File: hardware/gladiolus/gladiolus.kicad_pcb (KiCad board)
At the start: 4 copper layers, 70.7 x 53.3 mm, 133 parts, among them J1 NEIGHBOR1, J2 NEIGHBOR2, J7 BONUS_ROW, P1 CONN_01X05, Q1 Q_NPN_BEC, U1 THS4520RGT, U2 AD8330ARQZ, U3 AD9283, U4 AD9704, U5 LMH6643

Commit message: Gladiolus: updated series resistor values to match those used at ShmooCon 2017
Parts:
- R38, R39, R40, R41, R42, R43, R44, R45: value 39 -> 0
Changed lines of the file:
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@@
   )
   (setup
-    (last_trace_width 1.27)
+    (last_trace_width 0.3048)
     (user_trace_width 0.3048)
     (user_trace_width 0.508)
@@
       (effects (font (size 0.6096 0.6096) (thickness 0.1524)))
     )
-    (fp_text value 39 (at 0 0) (layer F.SilkS) hide
+    (fp_text value 0 (at 0 0) (layer F.SilkS) hide
       (effects (font (size 0.6096 0.6096) (thickness 0.1524)))
     )
@@
       (effects (font (size 0.6096 0.6096) (thickness 0.1524)))
     )
-    (fp_text value 39 (at 0 0) (layer F.SilkS) hide
+    (fp_text value 0 (at 0 0) (layer F.SilkS) hide
       (effects (font (size 0.6096 0.6096) (thickness 0.1524)))
     )
@@
       (effects (font (size 0.6096 0.6096) (thickness 0.1524)))
     )
-    (fp_text value 39 (at 0 0) (layer F.SilkS) hide
+    (fp_text value 0 (at 0 0) (layer F.SilkS) hide
       (effects (font (size 0.6096 0.6096) (thickness 0.1524)))
     )
@@
       (effects (font (size 0.6096 0.6096) (thickness 0.1524)))
     )
-    (fp_text value 39 (at 0 0) (layer F.SilkS) hide
+    (fp_text value 0 (at 0 0) (layer F.SilkS) hide
       (effects (font (size 0.6096 0.6096) (thickness 0.1524)))
     )
@@
       (effects (font (size 0.6096 0.6096) (thickness 0.1524)))
     )
-    (fp_text value 39 (at 0 0) (layer F.SilkS) hide
+    (fp_text value 0 (at 0 0) (layer F.SilkS) hide
       (effects (font (size 0.6096 0.6096) (thickness 0.1524)))
     )
@@
       (effects (font (size 0.6096 0.6096) (thickness 0.1524)))
     )
-    (fp_text value 39 (at 0 0) (layer F.SilkS) hide
+    (fp_text value 0 (at 0 0) (layer F.SilkS) hide
       (effects (font (size 0.6096 0.6096) (thickness 0.1524)))
     )
@@
       (effects (font (size 0.6096 0.6096) (thickness 0.1524)))
     )
-    (fp_text value 39 (at 0 0) (layer F.SilkS) hide
+    (fp_text value 0 (at 0 0) (layer F.SilkS) hide
       (effects (font (size 0.6096 0.6096) (thickness 0.1524)))
     )
@@
       (effects (font (size 0.6096 0.6096) (thickness 0.1524)))
     )
-    (fp_text value 39 (at 0 0) (layer F.SilkS) hide
-      (effects (font (size 0.6096 0.6096) (thickness 0.1524)))
-    )
+    (fp_text value 0 (at 0 0) (layer F.SilkS) hide
+      (effects (font (size 0.6096 0.6096) (thickness 0.1524)))
+    )

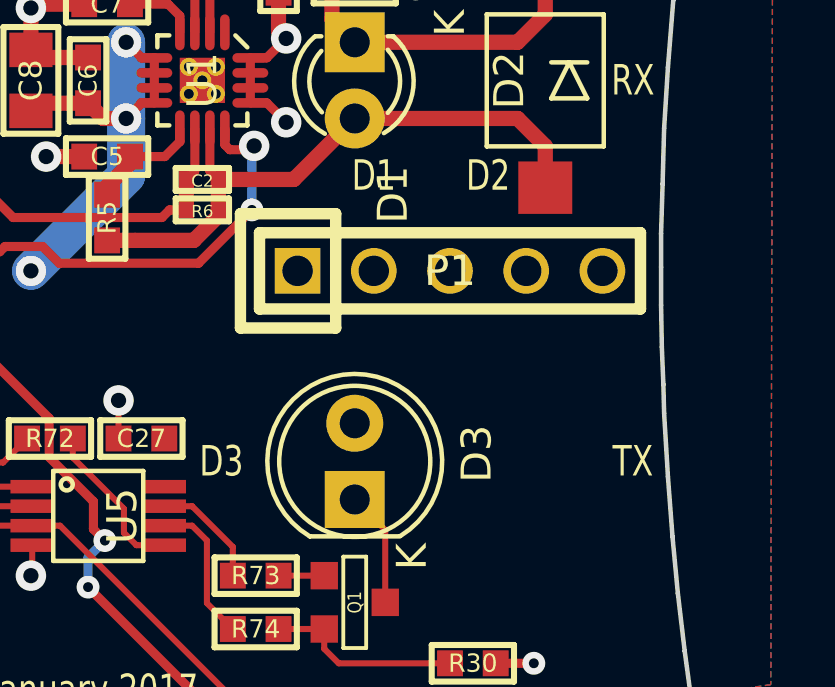
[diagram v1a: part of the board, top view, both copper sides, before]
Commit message: Gladiolus: added LED/photodiode expansion to P1
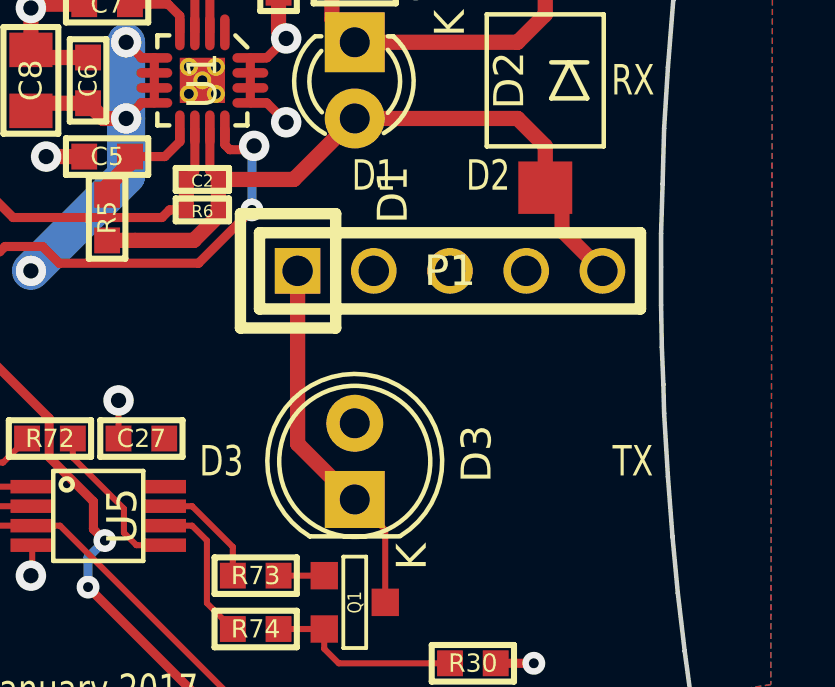
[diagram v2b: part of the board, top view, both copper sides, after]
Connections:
- C2 pad 2: Net-(C2-Pad2) -> /RXIN
- D1 pad 2: Net-(C2-Pad2) -> /RXIN
- D2 pad 2: Net-(C2-Pad2) -> /RXIN
- D3 pad 1: Net-(D3-Pad1) -> /TXOUT
- P1 pad 1: GND -> /TXOUT
- P1 pad 3: GND -> VCC
- P1 pad 5: GND -> /RXIN
- Q1 pad 3: Net-(D3-Pad1) -> /TXOUT
- R5 pad 1: Net-(C2-Pad2) -> /RXIN
- R6 pad 2: Net-(C2-Pad2) -> /RXIN
- U1 pad 11: Net-(C2-Pad2) -> /RXIN
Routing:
- net /RXIN: track 0.00 -> 24.1 mm
- net Net-(C2-Pad2): track 20.6 -> 0.00 mm
- net /TXOUT: track 0.00 -> 12.3 mm
- net Net-(D3-Pad1): track 3.85 -> 0.00 mm

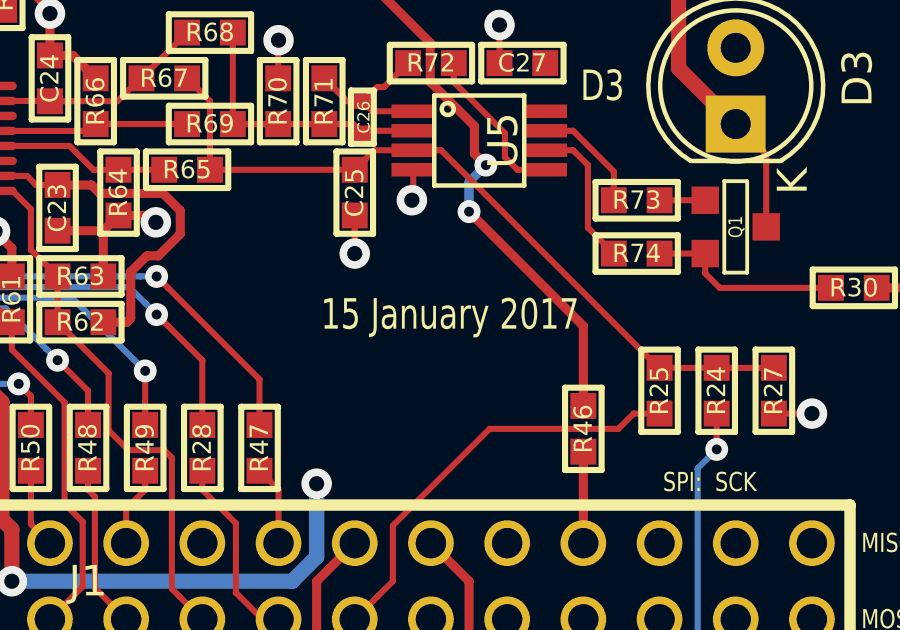
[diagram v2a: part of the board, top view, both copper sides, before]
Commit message: Gladiolus: updated date on silkscreen
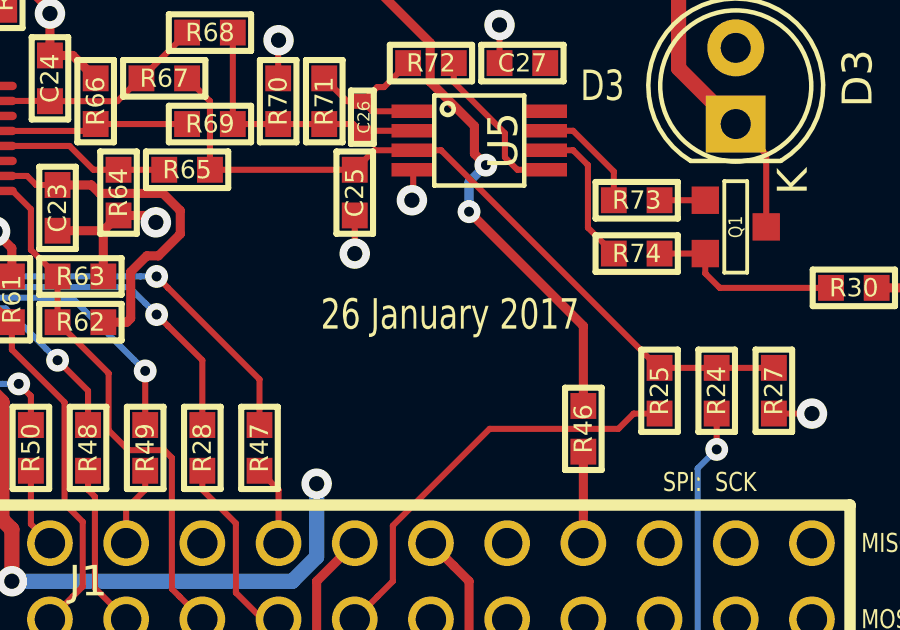
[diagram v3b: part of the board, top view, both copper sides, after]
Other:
- board text added: "26 January 2017"
- board text removed: "15 January 2017"
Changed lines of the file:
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@@
   (gr_line (start 177.9016 92.3544) (end 177.8508 94.0054) (angle 90) (layer Edge.Cuts) (width 0.15))
   (gr_line (start 177.9524 90.5002) (end 177.9016 92.3544) (angle 90) (layer Edge.Cuts) (width 0.15))
-  (gr_text "15 January 2017" (at 158.115 109.22) (layer F.SilkS)
+  (gr_text "26 January 2017" (at 158.115 109.22) (layer F.SilkS)
     (effects (font (size 1.016 0.762) (thickness 0.1524)))
   )

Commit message: Added part numbers for R57, R64, R66, R69, & R71; Changed values of R64, R66, & R69 to reflect part.
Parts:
- R64, R66, R69: value 250 -> 249
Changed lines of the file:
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@@
-(kicad_pcb (version 4) (host pcbnew 4.0.4-stable)
+(kicad_pcb (version 4) (host pcbnew 4.0.4+dfsg1-stable)
   (general
     (links 338)
@@
     (1 C2.Cu power hide)
     (2 C3.Cu power hide)
-    (31 B.Cu signal)
+    (31 B.Cu signal hide)
     (33 F.Adhes user)
     (35 F.Paste user)
@@
   )
   (setup
-    (last_trace_width 0.508)
+    (last_trace_width 0.2032)
     (user_trace_width 0.3048)
     (user_trace_width 0.508)
@@
       (effects (font (size 0.6096 0.6096) (thickness 0.1524)))
     )
-    (fp_text value 250 (at 0 0 270) (layer F.SilkS) hide
+    (fp_text value 249 (at 0 0 270) (layer F.SilkS) hide
       (effects (font (size 0.6096 0.6096) (thickness 0.1524)))
     )
@@
       (effects (font (size 0.6096 0.6096) (thickness 0.1524)))
     )
-    (fp_text value 250 (at 0 0 90) (layer F.SilkS) hide
+    (fp_text value 249 (at 0 0 90) (layer F.SilkS) hide
       (effects (font (size 0.6096 0.6096) (thickness 0.1524)))
     )
@@
       (effects (font (size 0.6096 0.6096) (thickness 0.1524)))
     )
-    (fp_text value 250 (at 0 0 180) (layer F.SilkS) hide
+    (fp_text value 249 (at 0 0 180) (layer F.SilkS) hide
       (effects (font (size 0.6096 0.6096) (thickness 0.1524)))
     )

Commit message: Gladiolus: changed R57 from 2k to 20k to bring DAC output current into supported range
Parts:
- R57: value 2k -> 20k
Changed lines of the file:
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@@
-(kicad_pcb (version 4) (host pcbnew 4.0.4+dfsg1-stable)
+(kicad_pcb (version 4) (host pcbnew 4.0.4-stable)
   (general
     (links 338)
@@
       (effects (font (size 0.6096 0.6096) (thickness 0.1524)))
     )
-    (fp_text value 2k (at 0 0 270) (layer F.SilkS) hide
-      (effects (font (size 0.6096 0.6096) (thickness 0.1524)))
-    )
+    (fp_text value 20k (at 0 0 270) (layer F.SilkS) hide
+      (effects (font (size 0.6096 0.6096) (thickness 0.1524)))
+    )

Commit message: Gladiolus: changed R70 and R71 values to shift common mode voltage of DAC amplifier output
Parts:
- R70: value 953 -> 1.80k
- R71: value 1000 -> 953
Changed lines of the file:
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@@
       (effects (font (size 0.6096 0.6096) (thickness 0.1524)))
     )
-    (fp_text value 1000 (at 0 0 90) (layer F.SilkS) hide
+    (fp_text value 953 (at 0 0 90) (layer F.SilkS) hide
       (effects (font (size 0.6096 0.6096) (thickness 0.1524)))
     )
@@
       (effects (font (size 0.6096 0.6096) (thickness 0.1524)))
     )
-    (fp_text value 953 (at 0 0 90) (layer F.SilkS) hide
+    (fp_text value 1.80k (at 0 0 90) (layer F.SilkS) hide
       (effects (font (size 0.6096 0.6096) (thickness 0.1524)))
     )

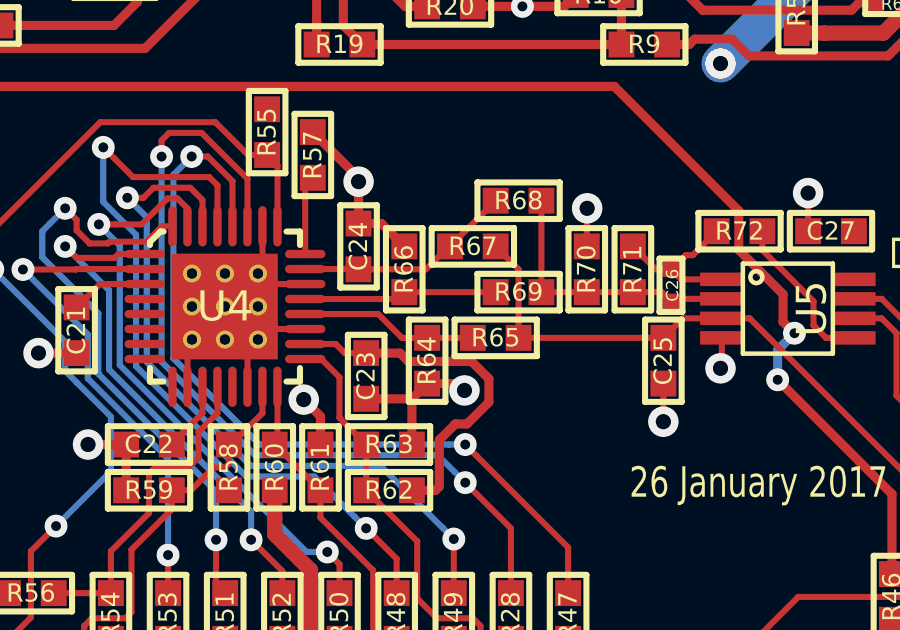
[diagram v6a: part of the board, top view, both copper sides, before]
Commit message: Gladiolus: inverted DAC output by swapping differential output pin connections
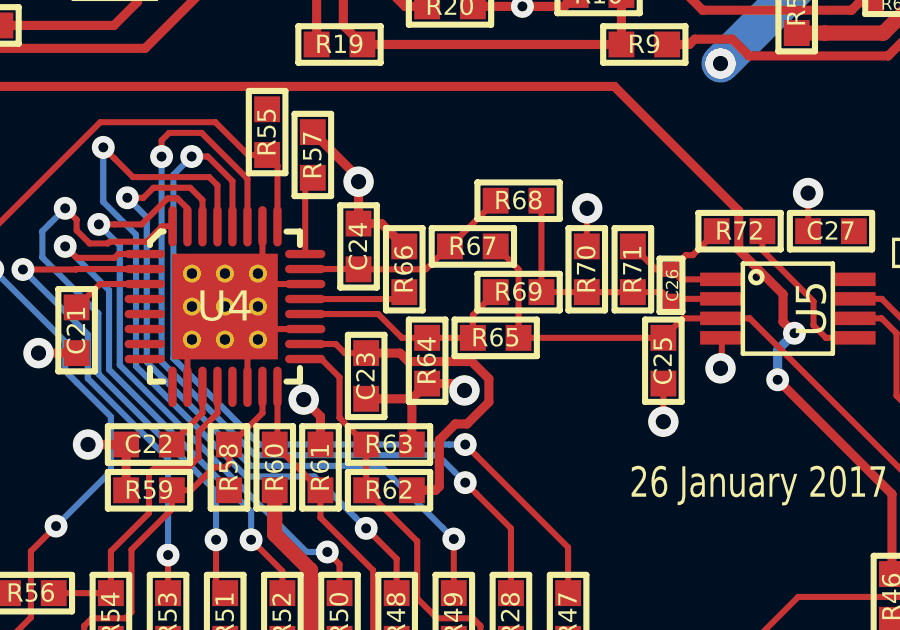
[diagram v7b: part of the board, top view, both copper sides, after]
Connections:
- R69 pad 2: Net-(R66-Pad1) -> Net-(R64-Pad1)
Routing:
- net Net-(R66-Pad1): track 6.45 -> 3.40 mm
- net Net-(R64-Pad1): track 5.92 -> 7.76 mm
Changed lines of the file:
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@@
     (links 338)
     (no_connects 0)
-    (area 109.525999 68.504999 180.415001 121.995001)
+    (area 107.95 66.04 279.525801 124.460001)
     (thickness 1.6)
     (drawings 130)
-    (tracks 902)
+    (tracks 903)
     (zones 0)
     (modules 133)
@@
     (fp_line (start 1.3716 0.6096) (end 1.3716 -0.6096) (layer F.SilkS) (width 0.2032))
     (pad 2 smd rect (at 0.762 0 180) (size 0.8636 0.8636) (layers F.Cu F.Paste F.Mask)
-      (net 155 "Net-(R66-Pad1)"))
+      (net 154 "Net-(R64-Pad1)"))
     (pad 1 smd rect (at -0.762 0 180) (size 0.8636 0.8636) (layers F.Cu F.Paste F.Mask)
       (net 143 "Net-(C26-Pad1)"))
@@
   (segment (start 143.002 101.6) (end 143.002 99.314) (width 0.2032) (layer F.Cu) (net 153))
   (segment (start 143.002 99.314) (end 143.256 99.06) (width 0.2032) (layer F.Cu) (net 153))
+  (segment (start 148.59 103.632) (end 149.352 102.87) (width 0.2032) (layer F.Cu) (net 154))
+  (segment (start 148.59 104.394) (end 148.59 103.632) (width 0.2032) (layer F.Cu) (net 154))
   (segment (start 145.4338 103.6) (end 146.2278 104.394) (width 0.2032) (layer F.Cu) (net 154))
   (segment (start 146.2278 104.394) (end 147.066 104.394) (width 0.2032) (layer F.Cu) (net 154))
@@
   (segment (start 143.002 103.1) (end 146.074 103.1) (width 0.2032) (layer F.Cu) (net 155))
   (segment (start 146.074 103.1) (end 146.304 102.87) (width 0.2032) (layer F.Cu) (net 155))
-  (segment (start 149.352 102.87) (end 146.304 102.87) (width 0.2032) (layer F.Cu) (net 155))
   (segment (start 160.3618 104.394) (end 159.945088 103.977288) (width 0.2032) (layer F.Cu) (net 156))
   (segment (start 159.945088 103.977288) (end 159.945088 103.176088) (width 0.2032) (layer F.Cu) (net 156))
